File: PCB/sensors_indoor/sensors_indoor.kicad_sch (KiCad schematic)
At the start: 16 parts, among them J1 USB4125-GF-A, U1 MIC5219-3.3YM5

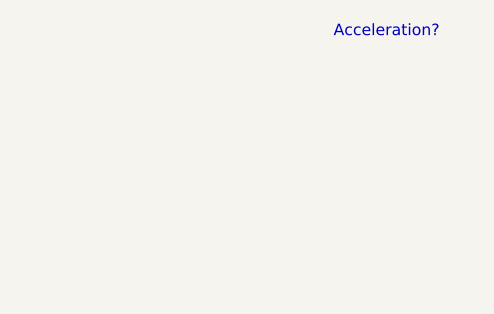
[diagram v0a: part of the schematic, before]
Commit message: Changed PTC fuse part
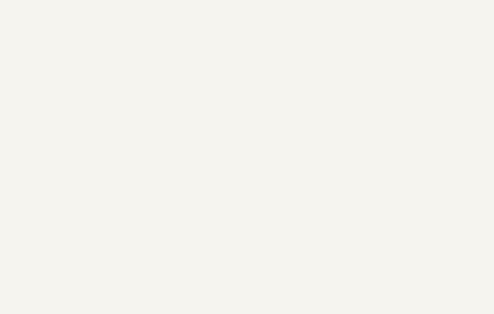
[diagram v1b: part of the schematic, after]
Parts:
- F1: footprint Fuse:Fuse_0805_2012Metric -> Fuse:Fuse_1206_3216Metric; MPN (none) -> MF-NSMF050-2; Mouser PN (none) -> 652-MF-NSMF050-2
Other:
- note removed: "Acceleration?"
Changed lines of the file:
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@@
 		(rev "A1")
-	)
-	(text "Acceleration?"
-		(exclude_from_sim no)
-		(at 267.716 17.526 0)
-		(effects
-			(font
-				(size 1.27 1.27)
-			)
-			(justify left)
-		)
 	)
 	(junction
@@
 			)
 		)
-		(property "Footprint" "Fuse:Fuse_0805_2012Metric"
+		(property "Footprint" "Fuse:Fuse_1206_3216Metric"
 			(at 101.6 40.64 0)
 			(effects
@@
 			(at 96.52 41.91 90)
 			(effects
+				(font
+					(size 1.27 1.27)
+				)
+				(hide yes)
+			)
+		)
+		(property "MPN" "MF-NSMF050-2"
+			(at 96.52 41.91 90)
+			(effects
+				(font
+					(size 1.27 1.27)
+				)
+				(hide yes)
+			)
+		)
+		(property "Mouser PN" "652-MF-NSMF050-2"
+			(at 96.52 41.91 90)
+			(effects
